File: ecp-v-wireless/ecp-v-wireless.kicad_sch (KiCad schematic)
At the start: 2 parts, among them U1 ESP32-S3-MINI-1, U2 LFE5U-85F-6BG381x

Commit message: Add schematic sheets and TODOs
Signed-off-by: Michael Welling <mwelling79@gmail.com>
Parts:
- removed U1: ESP32-S3-MINI-1, RF_Module:ESP32-S2-MINI-1, symbol RF_Module:ESP32-S3-MINI-1
- removed unit 9 of U2
- removed unit 1 of U2
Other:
- added sheet ESP32-S3 (ESP32-S3.kicad_sch)
- added sheet MISC-IO (MISC-IO.kicad_sch)
- added sheet POWER (POWER.kicad_sch)

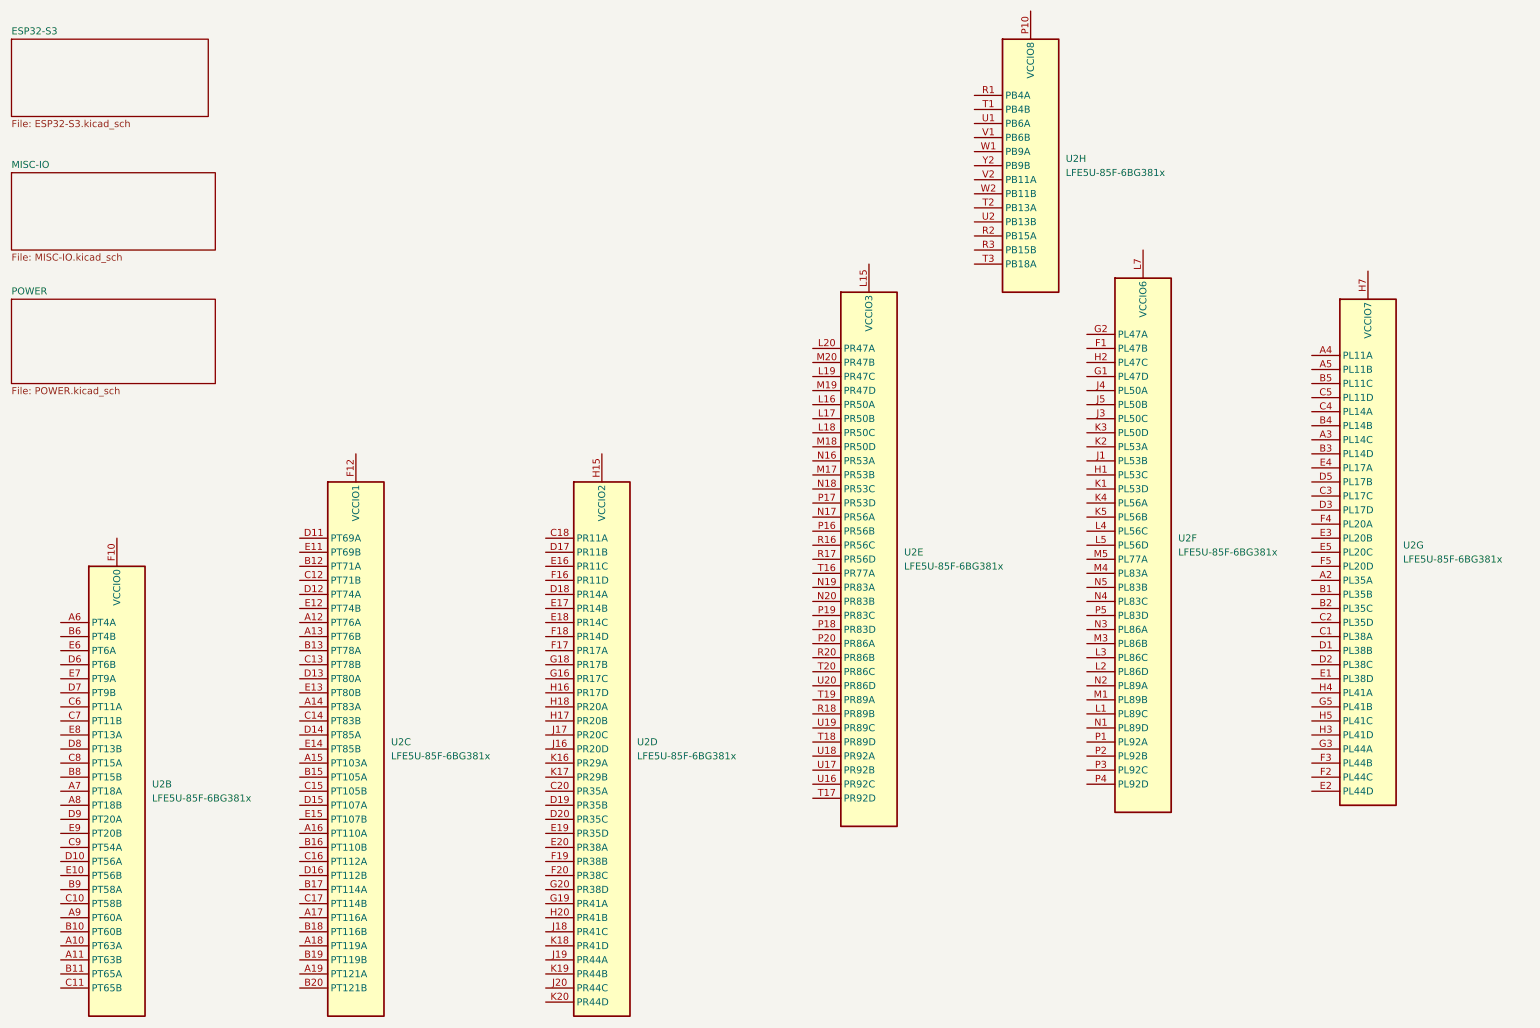
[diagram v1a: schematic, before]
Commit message: Add block diagram, USB, LiPo MGMT, Regs, etc
Signed-off-by: Michael Welling <mwelling79@gmail.com>
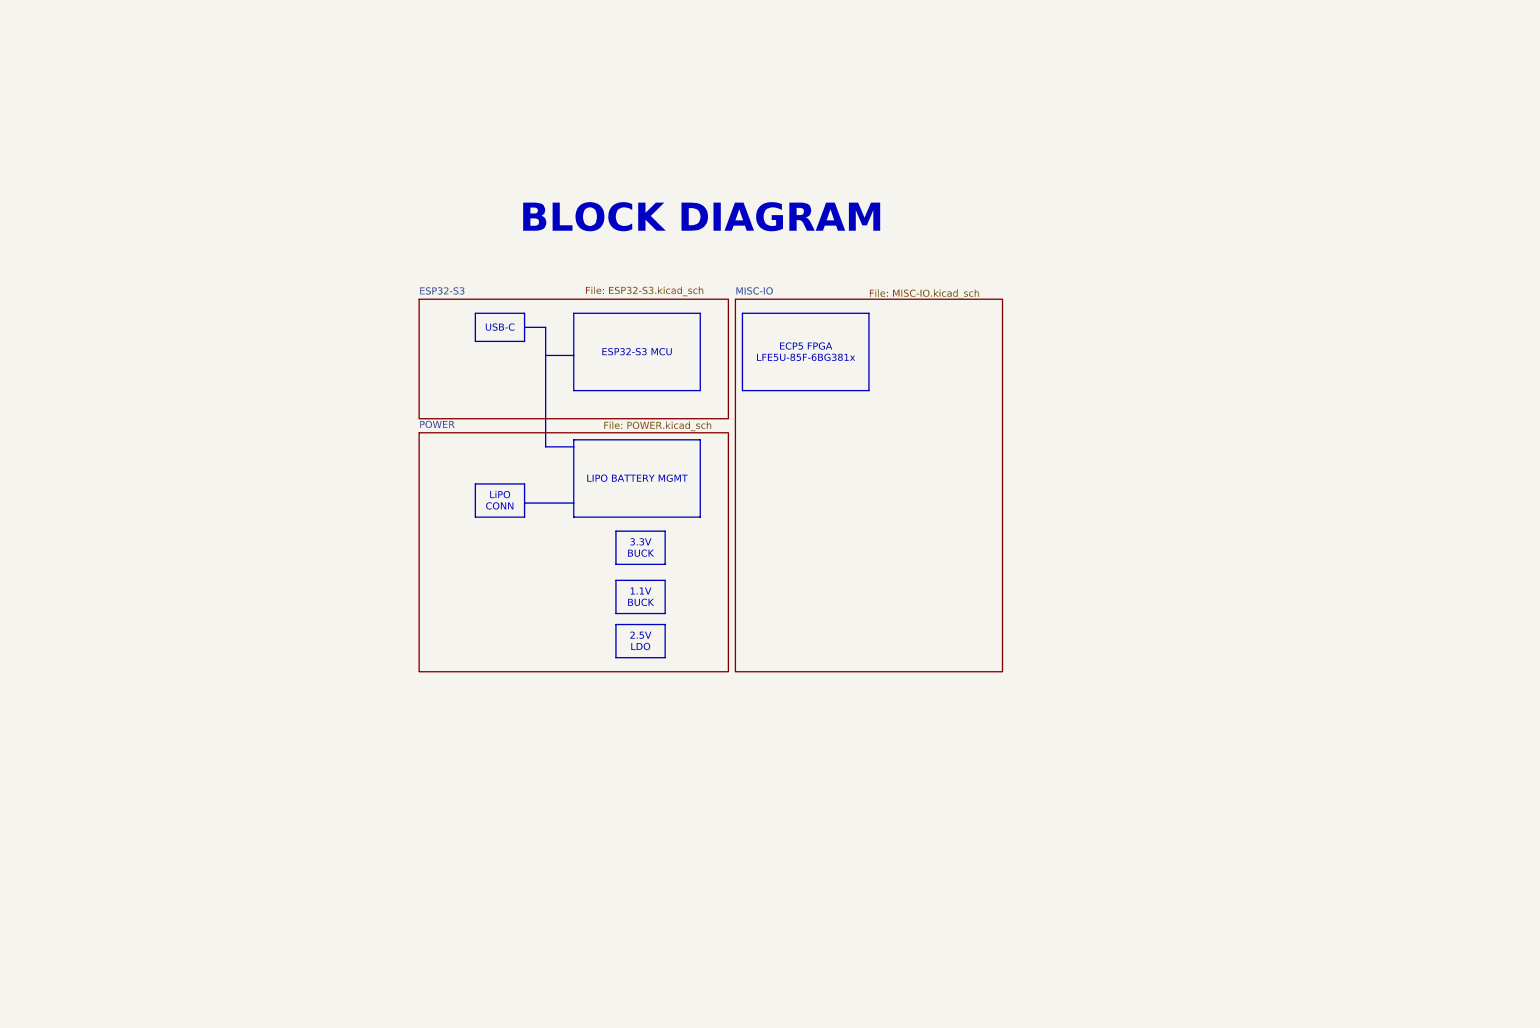
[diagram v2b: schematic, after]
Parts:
- removed U2: LFE5U-85F-6BG381x, Package_BGA:Lattice_caBGA-381_17x17mm_Layout20x20_P0.8mm, symbol FPGA_Lattice:LFE5U-85F-6BG381x
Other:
- note added: "BLOCK DIAGRAM"
